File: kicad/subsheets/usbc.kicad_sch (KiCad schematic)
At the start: 13 parts

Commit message: Resize sheets
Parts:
- R18, R19: value 5.1kOhm -> 5.1k
- R22: value 1 MOhm -> 1M
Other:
- moved on the sheet: C48, C49, D1, D2, D3, FB1, FB2, R18, R19, R20, R21, R22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

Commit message: Minor changes
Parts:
- D3: value D_TVS <1uF -> TVS Vr3.3 Vb4 <1uF
- renumbered C48 to C52, C49 to C53, R18 to R20, R19 to R21, R20 to R22, R21 to R23, R22 to R24
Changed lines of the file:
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@@
 		(on_board yes)
 		(dnp no)
-		(property "Reference" "#PWR029"
+		(property "Reference" "#PWR025"
 			(at 88.9 13.97 0)
 			(effects
@@
 			(project "srad-camera"
 				(path "/da62c771-e8c9-451f-8df1-ec995aadcb11/2d2335c5-b8ff-4d43-ae83-f45f6f125b07"
-					(reference "#PWR029")
+					(reference "#PWR025")
 					(unit 1)
 				)
@@
 		(on_board yes)
 		(dnp no)
-		(property "Reference" "R20"
+		(property "Reference" "R22"
 			(at 84.836 45.72 90)
 			(effects
@@
 			(project "srad-camera"
 				(path "/da62c771-e8c9-451f-8df1-ec995aadcb11/2d2335c5-b8ff-4d43-ae83-f45f6f125b07"
-					(reference "R20")
+					(reference "R22")
 					(unit 1)
 				)
@@
 		(on_board yes)
 		(dnp no)
-		(property "Reference" "C49"
+		(property "Reference" "C53"
 			(at 94.488 25.146 0)
 			(effects
@@
 			(project "srad-camera"
 				(path "/da62c771-e8c9-451f-8df1-ec995aadcb11/2d2335c5-b8ff-4d43-ae83-f45f6f125b07"
-					(reference "C49")
+					(reference "C53")
 					(unit 1)
 				)
@@
 			)
 		)
-		(property "Value" "D_TVS <1uF"
+		(property "Value" "TVS Vr3.3 Vb4 <1uF"
 			(at 85.344 64.2621 90)
 			(effects
@@
 		(on_board yes)
 		(dnp no)
-		(property "Reference" "C48"
+		(property "Reference" "C52"
 			(at 82.804 25.146 0)
 			(effects
@@
 			(project "srad-camera"
 				(path "/da62c771-e8c9-451f-8df1-ec995aadcb11/2d2335c5-b8ff-4d43-ae83-f45f6f125b07"
-					(reference "C48")
+					(reference "C52")
 					(unit 1)
 				)
@@
 		(on_board yes)
 		(dnp no)
-		(property "Reference" "R18"
+		(property "Reference" "R20"
 			(at 41.91 30.988 90)
 			(effects
@@
 			(project "srad-camera"
 				(path "/da62c771-e8c9-451f-8df1-ec995aadcb11/2d2335c5-b8ff-4d43-ae83-f45f6f125b07"
-					(reference "R18")
+					(reference "R20")
 					(unit 1)
 				)
@@
 		(on_board yes)
 		(dnp no)
-		(property "Reference" "#PWR030"
+		(property "Reference" "#PWR026"
 			(at 31.75 36.83 0)
 			(effects
@@
 			(project "srad-camera"
 				(path "/da62c771-e8c9-451f-8df1-ec995aadcb11/2d2335c5-b8ff-4d43-ae83-f45f6f125b07"
-					(reference "#PWR030")
+					(reference "#PWR026")
 					(unit 1)
 				)
@@
 		(dnp no)
 		(fields_autoplaced yes)
-		(property "Reference" "#PWR031"
+		(property "Reference" "#PWR027"
 			(at 80.01 73.66 0)
 			(effects
@@
 			(project "srad-camera"
 				(path "/da62c771-e8c9-451f-8df1-ec995aadcb11/2d2335c5-b8ff-4d43-ae83-f45f6f125b07"
-					(reference "#PWR031")
+					(reference "#PWR027")
 					(unit 1)
 				)
@@
 		(dnp no)
 		(fields_autoplaced yes)
-		(property "Reference" "#PWR032"
+		(property "Reference" "#PWR028"
 			(at 54.61 91.44 0)
 			(effects
@@
 			(project "srad-camera"
 				(path "/da62c771-e8c9-451f-8df1-ec995aadcb11/2d2335c5-b8ff-4d43-ae83-f45f6f125b07"
-					(reference "#PWR032")
+					(reference "#PWR028")
 					(unit 1)
 				)
@@
 		(on_board yes)
 		(dnp no)
-		(property "Reference" "R22"
+		(property "Reference" "R24"
 			(at 50.292 76.708 0)
 			(effects
@@
 			(project "srad-camera"
 				(path "/da62c771-e8c9-451f-8df1-ec995aadcb11/2d2335c5-b8ff-4d43-ae83-f45f6f125b07"
-					(reference "R22")
+					(reference "R24")
 					(unit 1)
 				)
@@
 		(on_board yes)
 		(dnp no)
-		(property "Reference" "R21"
+		(property "Reference" "R23"
 			(at 84.836 56.642 90)
 			(effects
@@
 			(project "srad-camera"
 				(path "/da62c771-e8c9-451f-8df1-ec995aadcb11/2d2335c5-b8ff-4d43-ae83-f45f6f125b07"
-					(reference "R21")
+					(reference "R23")
 					(unit 1)
 				)
@@
 		(on_board yes)
 		(dnp no)
-		(property "Reference" "R19"
+		(property "Reference" "R21"
 			(at 41.91 40.64 90)
 			(effects
@@
 			(project "srad-camera"
 				(path "/da62c771-e8c9-451f-8df1-ec995aadcb11/2d2335c5-b8ff-4d43-ae83-f45f6f125b07"
-					(reference "R19")
-					(unit 1)
-				)
+					(reference "R21")
+					(unit 1)
+				)

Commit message: Clean up root sheet, add power supply subsheet
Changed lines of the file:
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@@
 		)
 		(property "Value" "5.1k"
-			(at 35.814 32.766 90)
+			(at 41.275 32.639 90)
 			(effects
 				(font
@@
 		)
 		(property "Value" "5.1k"
-			(at 35.941 42.545 90)
-			(effects
-				(font
+			(at 41.402 42.418 90)
+			(effects
+				(font

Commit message: Add power supply and ll shifter
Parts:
- C53: value 0.1uF -> 100nF
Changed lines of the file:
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@@
 			)
 		)
-		(property "Value" "0.1uF"
+		(property "Value" "100nF"
 			(at 94.488 27.178 0)
 			(effects

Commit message: Annotations
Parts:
- renumbered C52 to C5, C53 to C6, R20 to R12, R21 to R13, R22 to R14, R23 to R15, R24 to R16
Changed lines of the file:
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@@
 		(on_board yes)
 		(dnp no)
-		(property "Reference" "#PWR025"
+		(property "Reference" "#PWR016"
 			(at 88.9 13.97 0)
 			(effects
@@
 			(project "srad-camera"
 				(path "/da62c771-e8c9-451f-8df1-ec995aadcb11/2d2335c5-b8ff-4d43-ae83-f45f6f125b07"
-					(reference "#PWR025")
+					(reference "#PWR016")
 					(unit 1)
 				)
@@
 		(on_board yes)
 		(dnp no)
-		(property "Reference" "R22"
+		(property "Reference" "R14"
 			(at 84.836 45.72 90)
 			(effects
@@
 			(project "srad-camera"
 				(path "/da62c771-e8c9-451f-8df1-ec995aadcb11/2d2335c5-b8ff-4d43-ae83-f45f6f125b07"
-					(reference "R22")
+					(reference "R14")
 					(unit 1)
 				)
@@
 		(on_board yes)
 		(dnp no)
-		(property "Reference" "C53"
+		(property "Reference" "C6"
 			(at 94.488 25.146 0)
 			(effects
@@
 			(project "srad-camera"
 				(path "/da62c771-e8c9-451f-8df1-ec995aadcb11/2d2335c5-b8ff-4d43-ae83-f45f6f125b07"
-					(reference "C53")
+					(reference "C6")
 					(unit 1)
 				)
@@
 		(on_board yes)
 		(dnp no)
-		(property "Reference" "C52"
+		(property "Reference" "C5"
 			(at 82.804 25.146 0)
 			(effects
@@
 			(project "srad-camera"
 				(path "/da62c771-e8c9-451f-8df1-ec995aadcb11/2d2335c5-b8ff-4d43-ae83-f45f6f125b07"
-					(reference "C52")
+					(reference "C5")
 					(unit 1)
 				)
@@
 		(on_board yes)
 		(dnp no)
-		(property "Reference" "R20"
+		(property "Reference" "R12"
 			(at 41.91 30.988 90)
 			(effects
@@
 			(project "srad-camera"
 				(path "/da62c771-e8c9-451f-8df1-ec995aadcb11/2d2335c5-b8ff-4d43-ae83-f45f6f125b07"
-					(reference "R20")
+					(reference "R12")
 					(unit 1)
 				)
@@
 		(on_board yes)
 		(dnp no)
-		(property "Reference" "#PWR026"
+		(property "Reference" "#PWR017"
 			(at 31.75 36.83 0)
 			(effects
@@
 			(project "srad-camera"
 				(path "/da62c771-e8c9-451f-8df1-ec995aadcb11/2d2335c5-b8ff-4d43-ae83-f45f6f125b07"
-					(reference "#PWR026")
+					(reference "#PWR017")
 					(unit 1)
 				)
@@
 		(dnp no)
 		(fields_autoplaced yes)
-		(property "Reference" "#PWR027"
+		(property "Reference" "#PWR018"
 			(at 80.01 73.66 0)
 			(effects
@@
 			(project "srad-camera"
 				(path "/da62c771-e8c9-451f-8df1-ec995aadcb11/2d2335c5-b8ff-4d43-ae83-f45f6f125b07"
-					(reference "#PWR027")
+					(reference "#PWR018")
 					(unit 1)
 				)
@@
 		(dnp no)
 		(fields_autoplaced yes)
-		(property "Reference" "#PWR028"
+		(property "Reference" "#PWR019"
 			(at 54.61 91.44 0)
 			(effects
@@
 			(project "srad-camera"
 				(path "/da62c771-e8c9-451f-8df1-ec995aadcb11/2d2335c5-b8ff-4d43-ae83-f45f6f125b07"
-					(reference "#PWR028")
+					(reference "#PWR019")
 					(unit 1)
 				)
@@
 		(on_board yes)
 		(dnp no)
-		(property "Reference" "R24"
+		(property "Reference" "R16"
 			(at 50.292 76.708 0)
 			(effects
@@
 			(project "srad-camera"
 				(path "/da62c771-e8c9-451f-8df1-ec995aadcb11/2d2335c5-b8ff-4d43-ae83-f45f6f125b07"
-					(reference "R24")
+					(reference "R16")
 					(unit 1)
 				)
@@
 		(on_board yes)
 		(dnp no)
-		(property "Reference" "R23"
+		(property "Reference" "R15"
 			(at 84.836 56.642 90)
 			(effects
@@
 			(project "srad-camera"
 				(path "/da62c771-e8c9-451f-8df1-ec995aadcb11/2d2335c5-b8ff-4d43-ae83-f45f6f125b07"
-					(reference "R23")
+					(reference "R15")
 					(unit 1)
 				)
@@
 		(on_board yes)
 		(dnp no)
-		(property "Reference" "R21"
+		(property "Reference" "R13"
 			(at 41.91 40.64 90)
 			(effects
@@
 			(project "srad-camera"
 				(path "/da62c771-e8c9-451f-8df1-ec995aadcb11/2d2335c5-b8ff-4d43-ae83-f45f6f125b07"
-					(reference "R21")
-					(unit 1)
-				)
+					(reference "R13")
+					(unit 1)
+				)

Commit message: Annotations + minor tweaks
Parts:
- R14, R15: value 22 Ohm -> 22

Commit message: Annotations + minor tweaks
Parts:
- added R46: 10k, symbol Device:R_Small
- added R52: 15k, symbol Device:R_Small
- R14, R15: value 22 -> 2.2R
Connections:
- net GND: now also R52.2
- net USB_5V: now reaches D1.1 (A1), FB1.2, USB1.A4 (VBUS), USB1.A9 (VBUS), USB1.B4 (VBUS), USB1.B9 (VBUS)
- net USB_5V: now also R46.2
- new net VBUSDET: R46.1, R52.1
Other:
- moved on the sheet: C5, C6, D1, D2, D3, FB1, FB2, R12, R13, R14, R15, R16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

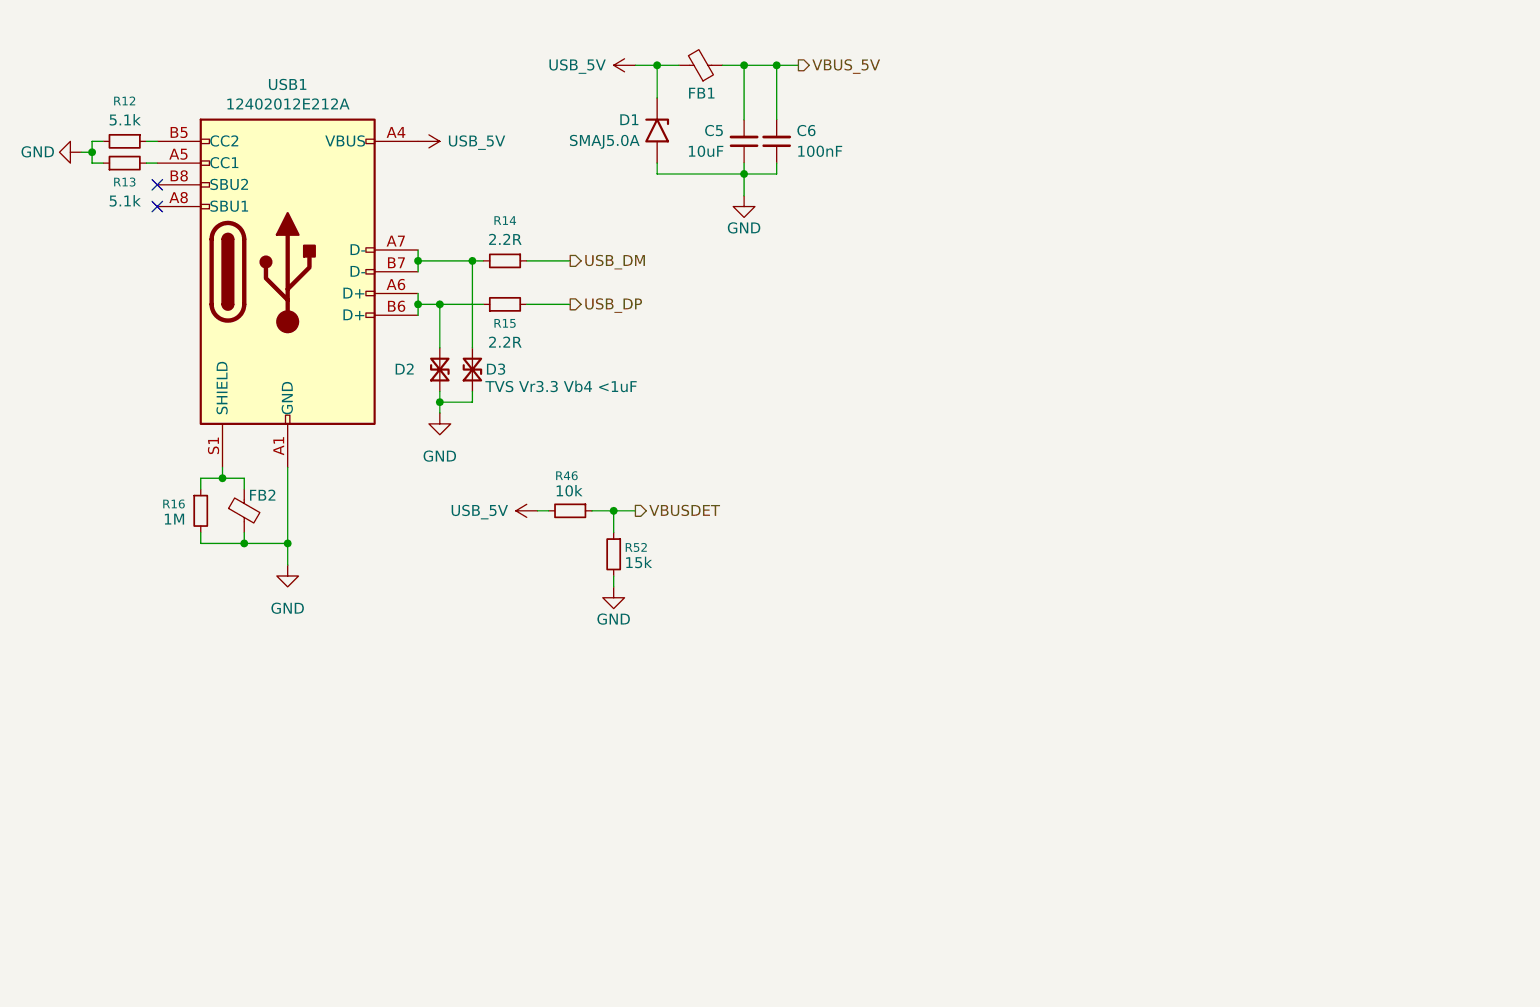
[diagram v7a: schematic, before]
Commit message: Change all sheets to A4, name sheets, split RK3566 into hierarchy
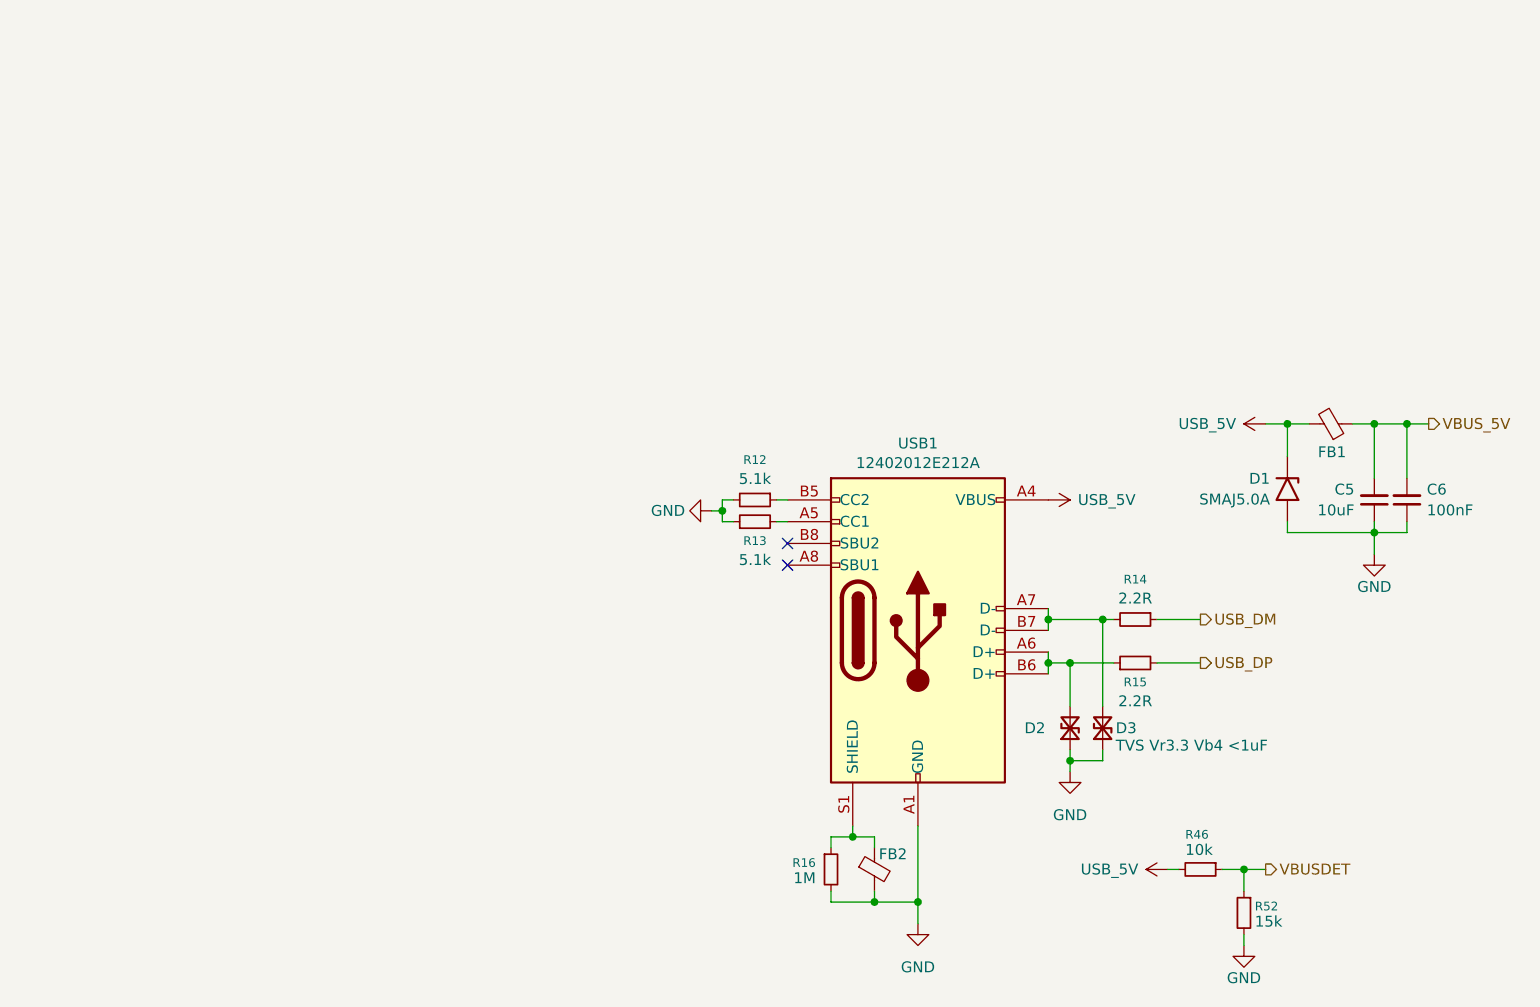
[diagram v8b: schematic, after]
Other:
- title: (none) -> USB C Port
- moved on the sheet: C5, C6, D1, D2, D3, FB1, FB2, R12, R13, R14, R15, R16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
